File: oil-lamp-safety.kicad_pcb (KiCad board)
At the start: 2 copper layers, 45 x 65 mm, 31 parts, among them J1 Screw_Terminal_01x09, Q1 IRF540N, Q2 IRF540N, Q3 IRF540N, U1 HEF4093B

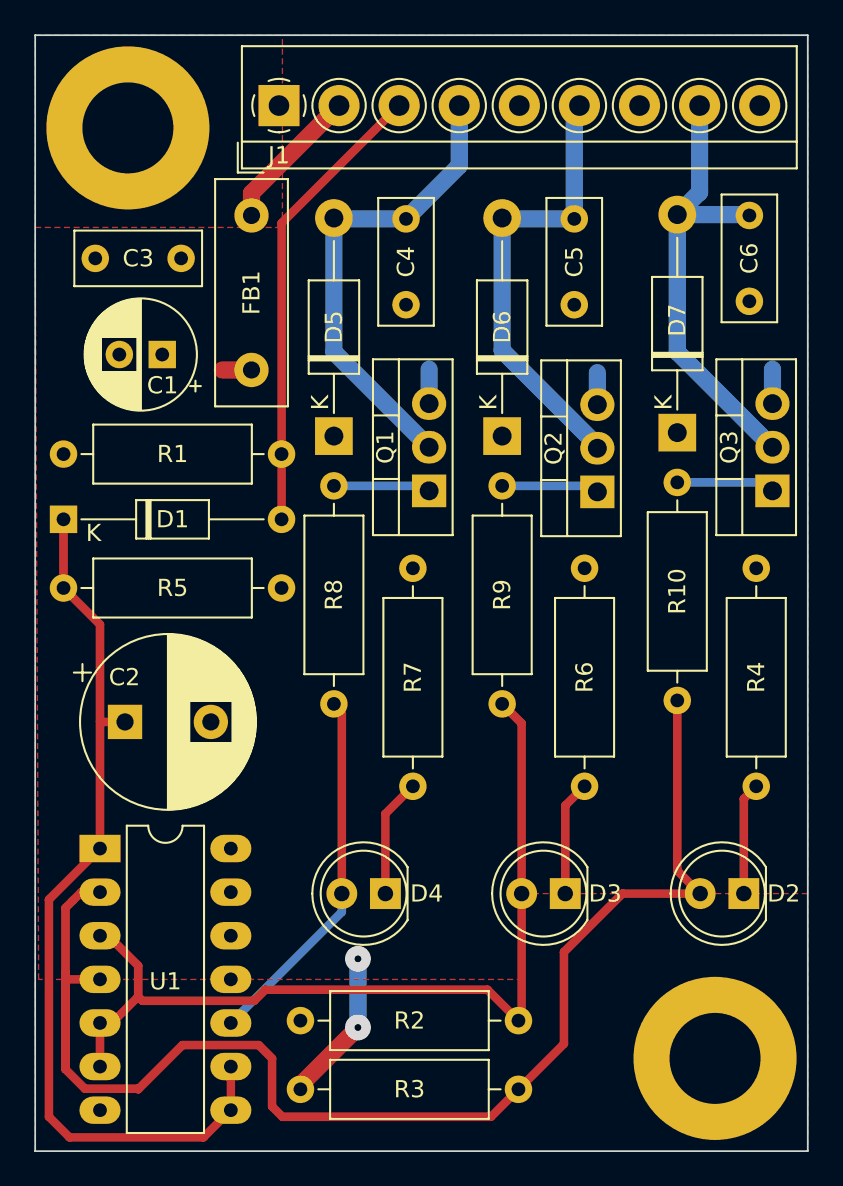
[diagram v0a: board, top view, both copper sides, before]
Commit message: Updated the design to fix lockout on power up issue.
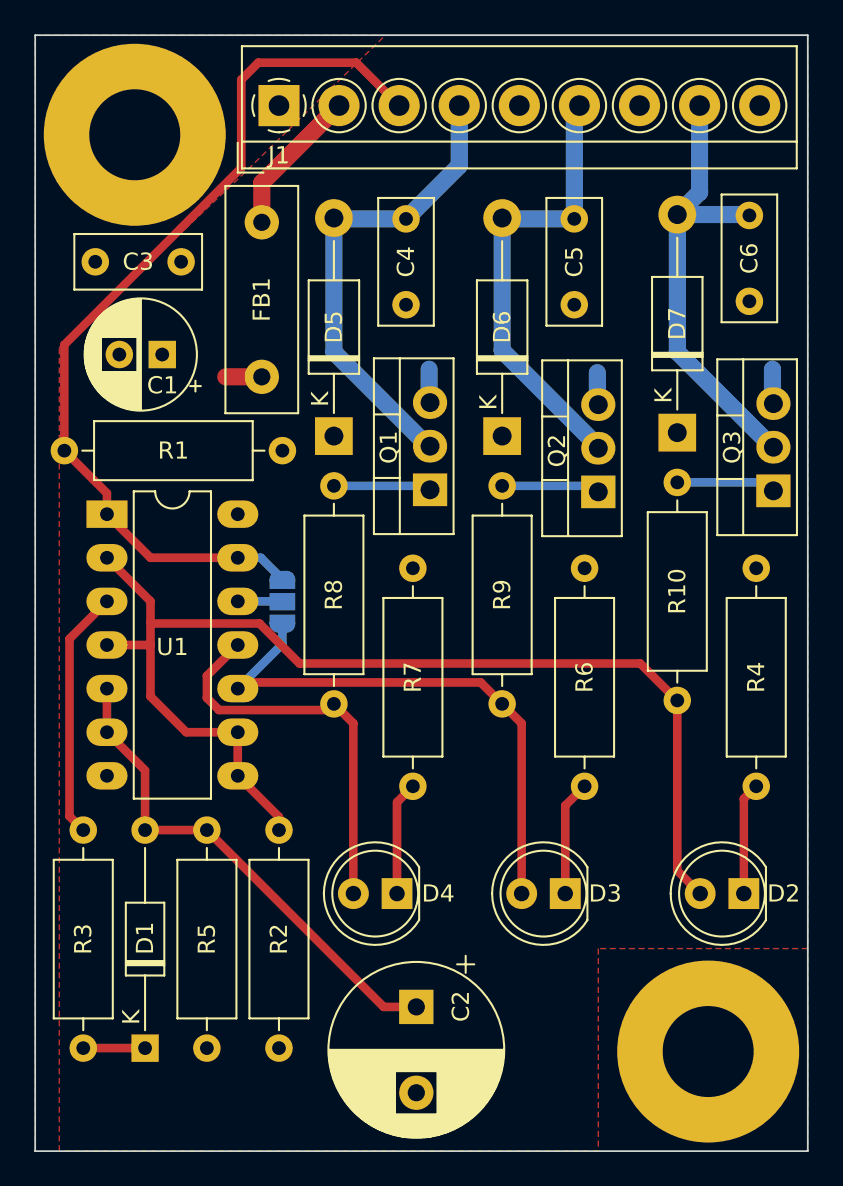
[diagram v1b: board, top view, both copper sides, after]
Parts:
- removed REF** (x2): MountingHole_5.3mm_M5_ISO7380_Pad, MountingHole:MountingHole_5.3mm_M5_ISO7380_Pad
- added H1: MountingHole_Pad, MountingHole:MountingHole_5.3mm_M5_Pad, F.Cu at (85.8, 65.8)
- added H2: MountingHole_Pad, MountingHole:MountingHole_5.3mm_M5_Pad, F.Cu at (119.2, 119.2)
- added JP1: SolderJumper_3_Open, Jumper:SolderJumper-3_P1.3mm_Open_RoundedPad1.0x1.5mm, B.Cu at (94.4, 93.0)
- moved D1 31.2 mm to (86.4, 119.0), turned to 90 degrees
- moved R5 28.1 mm to (90.0, 119.0), turned to 90 degrees
- moved C2 23.7 mm to (102.2, 116.6), turned to -90 degrees
- moved R3 19.7 mm to (82.8, 106.3), turned to -90 degrees
- moved U1 19.5 mm to (84.2, 87.9)
- moved R2 14.0 mm to (94.2, 119.0), turned to 90 degrees
- moved R1 12.8 mm to (94.4, 84.2), turned to 180 degrees
- moved FB1 9.42 mm to (93.2, 79.9), turned to 90 degrees
- moved D4 0.67 mm to (101.1, 110.0)
- moved C3 0.20 mm to (88.5, 73.2)
- moved Q1 0.08 mm to (103.0, 86.5)
- moved Q3 0.06 mm to (123.0, 86.5)
- moved Q2 0.05 mm to (112.8, 86.6)
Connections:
- C1 pad 1: OIL_BUZZER_OUT_12V -> +12V
- C1 pad 2: 12V_GND -> GND
- C2 pad 1: Net-(C2-Pad1) -> Net-(D1-A)
- C2 pad 2: 12V_GND -> GND
- C3 pad 1: OIL_BUZZER_OUT_12V -> +12V
- C3 pad 2: 12V_GND -> GND
- C4 pad 1: OIL_BUZZER_OUT_12V -> +12V
- C5 pad 1: OIL_BUZZER_OUT_12V -> +12V
- C6 pad 1: OIL_BUZZER_OUT_12V -> +12V
- D1 pad 1: Net-(C2-Pad1) -> Net-(D1-K)
- D1 pad 2: OIL_LOW_SIGNAL -> Net-(D1-A)
- D5 pad 1: OIL_BUZZER_OUT_12V -> +12V
- D6 pad 1: OIL_BUZZER_OUT_12V -> +12V
- D7 pad 1: OIL_BUZZER_OUT_12V -> +12V
- FB1 pad 1: 12V_BATT -> +12V
- FB1 pad 2: OIL_BUZZER_OUT_12V -> 12V_BATT
- J1 pad 1: 12V_GND -> GND
- J1 pad 5: OIL_BUZZER_OUT_12V -> +12V
- J1 pad 7: OIL_BUZZER_OUT_12V -> +12V
- J1 pad 9: OIL_BUZZER_OUT_12V -> +12V
- Q1 pad 3: 12V_GND -> GND
- Q2 pad 3: 12V_GND -> GND
- Q3 pad 3: 12V_GND -> GND
- R1 pad 1: OIL_BUZZER_OUT_12V -> +12V
- R2 pad 1: LOCKOUT -> +12V
- R2 pad 2: 12V_GND -> RUN
- R3 pad 1: OIL_BUZZER_OUT_12V -> Net-(R3-Pad1)
- R3 pad 2: RUN -> Net-(D1-K)
- R4 pad 2: 12V_GND -> GND
- R5 pad 1: Net-(C2-Pad1) -> +12V
- R5 pad 2: 12V_GND -> Net-(D1-A)
- R6 pad 2: 12V_GND -> GND
- R7 pad 2: 12V_GND -> GND
- U1 pad 1: Net-(C2-Pad1) -> OIL_LOW_SIGNAL
- U1 pad 10: OIL_LOW -> LOCKOUT
- U1 pad 11: unconnected-(U1-Pad11) -> OIL_LOW
- U1 pad 12: 12V_GND -> Net-(JP1-C)
- U1 pad 13: 12V_GND -> OIL_LOW_SIGNAL
- U1 pad 14: OIL_BUZZER_OUT_12V -> +12V
- U1 pad 3: LOCKOUT -> Net-(R3-Pad1)
- U1 pad 5: LOCKOUT -> Net-(D1-A)
- U1 pad 6: LOCKOUT -> Net-(D1-A)
- U1 pad 7: 12V_GND -> GND
- U1 pad 8: Net-(C2-Pad1) -> RUN
- U1 pad 9: Net-(C2-Pad1) -> RUN
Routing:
- net Net-(C2-Pad1): track 52.7 -> 0.00 mm
- net Net-(D1-A): track 0.00 -> 29.2 mm
- net OIL_LOW_SIGNAL: track 26.9 -> 53.0 mm
- net LOCKOUT: track 52.4 -> 32.4 mm
- net Net-(R3-Pad1): track 0.00 -> 14.6 mm
- net RUN: track 81.7 -> 68.7 mm
- net OIL_BUZZER_OUT_12V: track 10.7 -> 0.00 mm, vias 2 -> 0
- net GND: track 0.00 -> 5.87 mm
- net 12V_GND: track 5.87 -> 0.00 mm
- net Net-(D1-K): track 0.00 -> 3.60 mm
- net Net-(JP1-C): track 0.00 -> 2.61 mm
- net +12V: track 0.00 -> 2.10 mm
- net OIL_LOW: track 21.5 -> 23.2 mm
- added copper zone on F.Cu, net +12V
- added copper zone on B.Cu, net GND
- removed copper zone on B.Cu, net 12V_GND
- removed copper zone on F.Cu, net OIL_BUZZER_OUT_12V
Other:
- board text added: "BUZZER ALWAYS RUN ONLY"
- board text added: "OIL LAMP SAFETY V0.2"
- board text removed: "OIL LAMP SAFETY V0.1"
